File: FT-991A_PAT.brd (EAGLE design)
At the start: 44.6 x 59.8 mm, 24 parts, among them Q1 J310, Q2 BFS17

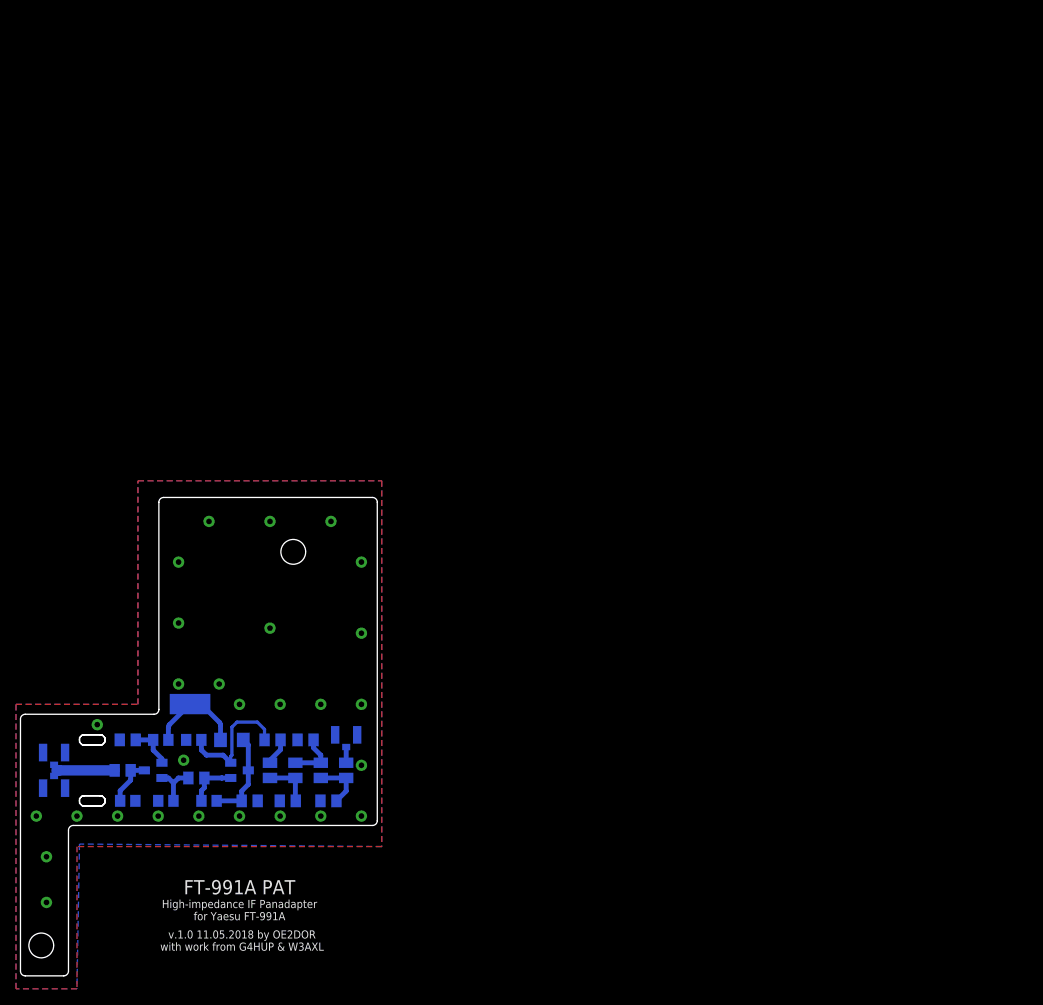
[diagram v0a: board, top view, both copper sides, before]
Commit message: Revision E
 - Now sports a RF switch (PE4259) instead of a regular Analog switch
   (was: SN74LVC1G66);
   * Also contains its resistors as per reference design;
- Changed voltage from 5V to 3.3V to Switch and AND port;
- SDR output will be grounded by default when switch is in default state
  (RF 2 port) port
- Updated list of contributors in Silk Screen.
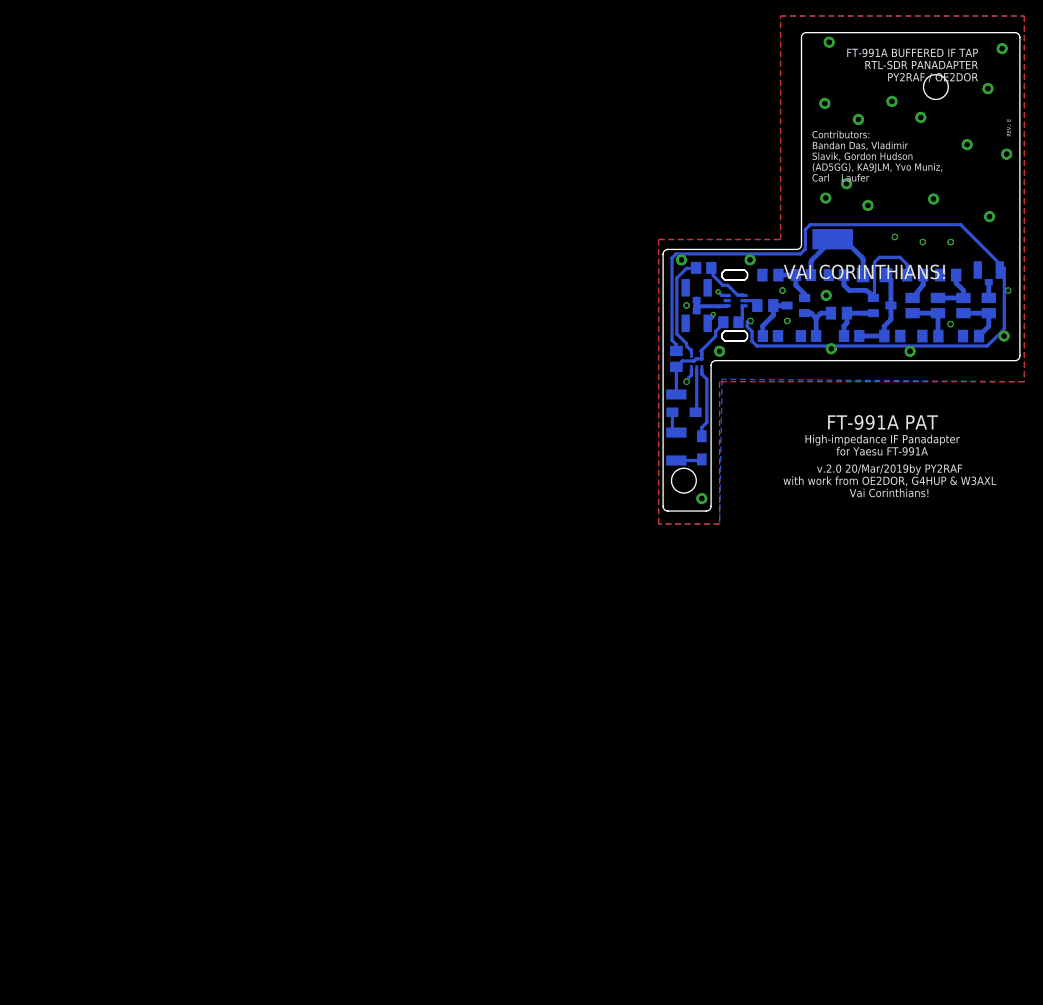
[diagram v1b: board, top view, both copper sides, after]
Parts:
- removed U$1: (no value), adafruit:U.FL
- added +3.3V, GPIO, SCPON: (no value), wirepad:SMD1,27-2,54
- added C9: 0.1uF, rcl:C0805K
- added D1, D2: 1SS355VM, diode:SOD323-W
- added R7, R8: 1k, rcl:R0805
- added S1: PE4259, psemi:SC-70
- added TAP_OUT: TAP_OUT, adafruit:U.FL
- added U2: SN74AHC1G08_DCK_5, sn74ahc1g08-dck:DCK5
- X1: value (none) -> SCP_OUT
- X2: value (none) -> IF_IN
- moved C1 99.1 mm to (43.5, 65.1)
- moved C2 99.1 mm to (44.1, 68.9)
- moved C3 99.1 mm to (52.7, 64.1)
- moved C4 99.1 mm to (59.4, 61.3)
- moved C5 99.1 mm to (62.2, 68.9)
- moved C6 99.1 mm to (64.1, 61.3)
- moved C7 99.1 mm to (66.4, 68.9)
- moved C8 99.1 mm to (69.2, 61.3)
- moved L1 99.1 mm to (61.9, 65.1)
- moved L2 99.1 mm to (65.1, 65.1)
- moved L3 99.1 mm to (68.3, 65.1)
- moved L4 99.1 mm to (71.4, 65.1)
- moved PAD1 99.1 mm to (51.9, 73.4)
- moved Q1 99.1 mm to (47.3, 65.1)
- moved Q2 99.1 mm to (58.1, 65.1)
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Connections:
- removed net N$14: C1.1, X1.3, X2.3
- new net N$15: C1.1, S1.5
- new net N$16: D1.A, GPIO.1
- new net N$17: D1.C, U2.2
- new net N$18: D2.A, SCPON.1
- new net N$19: R8.2, S1.4
- new net N$20: D2.C, U2.1
- new net N$22: R8.1, U2.4
- new net N$7: S1.1, X1.3, X2.3
- new net VCC: +3.3V.1, C9.1, R7.1, U2.5
- new net VDD: R7.2, S1.6
- net GNDA: now also C9.2, S1.2, S1.3, TAP_OUT.1, TAP_OUT.2, U2.3; no longer U$1.1, U$1.2
- net N$12: now also TAP_OUT.3; no longer U$1.3
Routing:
- net GNDA: track 0.00 -> 106.2 mm, vias 28 -> 34
- net N$22: track 0.00 -> 13.1 mm
- net VCC: track 0.00 -> 12.8 mm
- net N$14: track 10.4 -> 0.00 mm
- net N$20: track 0.00 -> 8.84 mm
- net N$19: track 0.00 -> 6.01 mm
- net N$17: track 0.00 -> 5.37 mm
- net N$7: track 0.00 -> 5.23 mm
- net N$18: track 0.00 -> 3.23 mm
- net N$16: track 0.00 -> 2.75 mm
- net VDD: track 0.00 -> 2.40 mm
- net N$15: track 0.00 -> 1.92 mm
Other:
- board text added: "+9V"
- board text added: "0.1 uF"
- board text added: "3.3V"
- board text added: ">PLOT_DATE_TIME"
- board text added: "Contributors: Bandan Das, Vladimir Slavik, Gordon Hudson (AD5GG), KA9JLM, Yvo Muniz, Carl Laufer"
- board text added: "FT-991A BUFFERED IF TAP RTL-SDR PANADAPTER PY2RAF / OE2DOR"
- board text added: "IF_IN"
- board text added: "REV.: E"
- board text added: "SCPOUT"
- board text added: "SDR OUT"
- board text added: "SIG"
- board text added: "VAI CORINTHIANS!"
- board text added: "v.2.0 20/Mar/2019by PY2RAF with work from OE2DOR, G4HUP & W3AXL Vai Corinthians!"
- board text removed: "FT-991A PAT v1.0 11.05.2018 OE2DOR"
- board text removed: "IF"
- board text removed: "IN/OUT"
- board text removed: "RF OUT"
- board text removed: "v.1.0 11.05.2018 by OE2DOR with work from G4HUP & W3AXL"

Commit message: Revision F
* Added 1 nF capacitors in RF lines in PE4529 (except RF2, goes with a
  470 pF to GND)
* Got rid of the VCC via which was crossing the RF line (argh)
* Finally got the courage to change a bit the board layout and escape
  from the thin strip that I was working previously.
* And another THANK YOU to Gordon AD5GG for his invaluable feedback and
  help.
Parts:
- removed C9: 0.1uF, rcl:C0805K
- added C10, C11: 1nF, rcl:C0805K
- added C13: 0.1uF, rcl:C0805K
- added C14: 470nF, rcl:C0805K
- GPIO: value (none) -> GPIO
- SCPON: value (none) -> SCPON
- moved GPIO 40.6 mm to (50.8, 85.4)
- moved SCPON 40.6 mm to (50.8, 81.9)
- moved D1 39.9 mm to (54.9, 85.4)
- moved D2 39.6 mm to (54.9, 81.8), turned to 0 degrees
- moved U2 32.2 mm to (59.3, 79.1), turned to 270 degrees
- moved +3.3V 30.9 mm to (50.6, 79.0)
- moved R7 28.6 mm to (64.4, 76.6)
- moved R8 23.0 mm to (58.2, 75.2), turned to 270 degrees
- moved X2 2.84 mm to (33.1, 60.7)
- moved X1 2.41 mm to (33.1, 65.7)
- moved S1 2.40 mm to (37.4, 65.7)
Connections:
- new net N$14: C1.1, C10.1
- new net N$21: C11.2, S1.1
- new net N$24: C14.2, S1.3
- net GNDA: now also C13.2, C14.1; no longer C9.2, S1.3
- net N$15: now also C10.2; no longer C1.1
- net N$7: now also C11.1; no longer S1.1
- net VCC: now also C13.1; no longer C9.1
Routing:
- net GNDA: track 106.2 -> 0.96 mm, vias 34 -> 35
- net VDD: track 2.40 -> 59.0 mm
- net N$19: track 6.01 -> 28.3 mm
- net N$22: track 13.1 -> 2.65 mm
- net N$20: track 8.84 -> 3.02 mm
- net N$24: track 0.00 -> 3.68 mm
- net N$14: track 0.00 -> 2.72 mm
- net VCC: track 12.8 -> 15.1 mm
- net N$21: track 0.00 -> 2.05 mm
- net N$7: track 5.23 -> 3.67 mm
- net N$17: track 5.37 -> 6.43 mm
- net N$18: track 3.23 -> 2.69 mm
- net N$15: track 1.92 -> 2.42 mm
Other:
- board text added: "100R"
- board text added: "220R"
- board text added: "Contributors: Bandan Das, Vladimir Slavik, Gordon Hudson \\o/ (AD5GG), KA9JLM, Yvo Muniz, Carl Laufer"
- board text added: "GPIO"
- board text added: "REV.: F"
- board text added: "SCPON"
- board text removed: "0.1 uF"
- board text removed: "100Ω"
- board text removed: "220"
- board text removed: "Contributors: Bandan Das, Vladimir Slavik, Gordon Hudson (AD5GG), KA9JLM, Yvo Muniz, Carl Laufer"
- board text removed: "REV.: E"
- board text removed: "SIG"

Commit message: New files, correction, better schematic layout
Still in Revision F:
* Fixed C14 values (it is 4.7 nF and not 470 pF)
* Cleaner and unified board layout
* Identified properly Q1 (it is a J310)
* A few tweaks and spam in board silk screen
* Added project's PDF and board's PNG images
... And that's all, folks! \o
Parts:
- C14: value 470nF -> 4.7nF
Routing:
- net GNDA: track 0.96 -> 1.84 mm, vias 35 -> 44
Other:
- board text added: "BFS17"
- board text added: "FT-991A BUFFERED IF TAP"
- board text added: "J310"
- board text added: "PY2RAF"
- board text added: "and"
- board text added: "rfsw"
- board text removed: "Q1"
